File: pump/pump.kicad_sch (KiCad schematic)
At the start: 0 parts

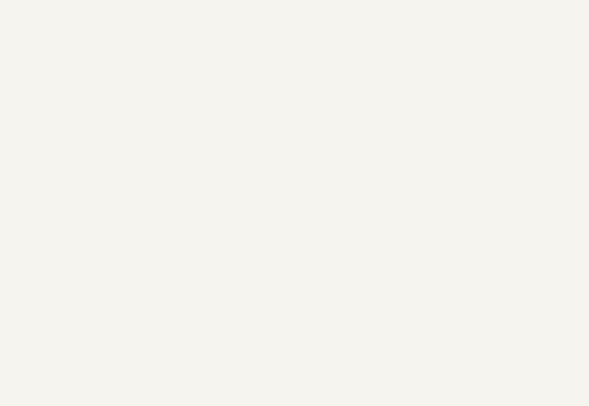
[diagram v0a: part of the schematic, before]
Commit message: Added control relays schematic
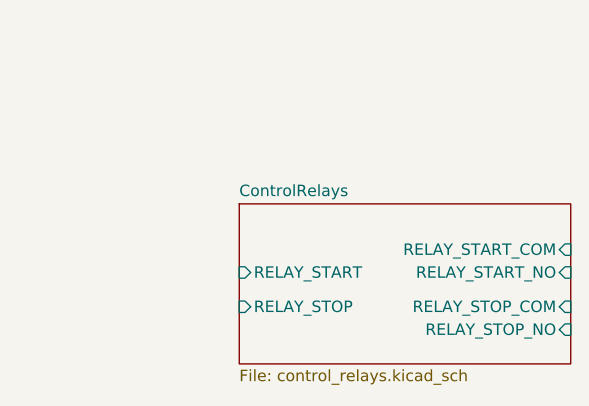
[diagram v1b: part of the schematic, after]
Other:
- added sheet ControlRelays (control_relays.kicad_sch)
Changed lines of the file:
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@@
+		)
+	)
+	(sheet
+		(at 228.6 144.78)
+		(size 36.83 17.78)
+		(exclude_from_sim no)
+		(in_bom yes)
+		(on_board yes)
+		(dnp no)
+		(fields_autoplaced yes)
+		(stroke
+			(width 0.1524)
+			(type solid)
+		)
+		(fill
+			(color 0 0 0 0.0000)
+		)
+		(property "Sheetname" "ControlRelays"
+			(at 228.6 144.0684 0)
+			(effects
+				(font
+					(size 1.27 1.27)
+				)
+				(justify left bottom)
+			)
+		)
+		(property "Sheetfile" "control_relays.kicad_sch"
+			(at 228.6 163.1446 0)
+			(effects
+				(font
+					(size 1.27 1.27)
+				)
+				(justify left top)
+			)
+		)
+		(pin "RELAY_START" input
+			(at 228.6 152.4 180)
+			(effects
+				(font
+					(size 1.27 1.27)
+				)
+				(justify left)
+			)
+		)
+		(pin "RELAY_START_COM" input
+			(at 265.43 149.86 0)
+			(effects
+				(font
+					(size 1.27 1.27)
+				)
+				(justify right)
+			)
+		)
+		(pin "RELAY_START_NO" input
+			(at 265.43 152.4 0)
+			(effects
+				(font
+					(size 1.27 1.27)
+				)
+				(justify right)
+			)
+		)
+		(pin "RELAY_STOP" input
+			(at 228.6 156.21 180)
+			(effects
+				(font
+					(size 1.27 1.27)
+				)
+				(justify left)
+			)
+		)
+		(pin "RELAY_STOP_COM" input
+			(at 265.43 156.21 0)
+			(effects
+				(font
+					(size 1.27 1.27)
+				)
+				(justify right)
+			)
+		)
+		(pin "RELAY_STOP_NO" input
+			(at 265.43 158.75 0)
+			(effects
+				(font
+					(size 1.27 1.27)
+				)
+				(justify right)
+			)
+		)
+		(instances
+			(project "pump"
+				(path "/e0be0fc6-35a9-4dbe-8638-3e88dcb86763"
+					(page "2")
+				)
+			)
 		)
 	)

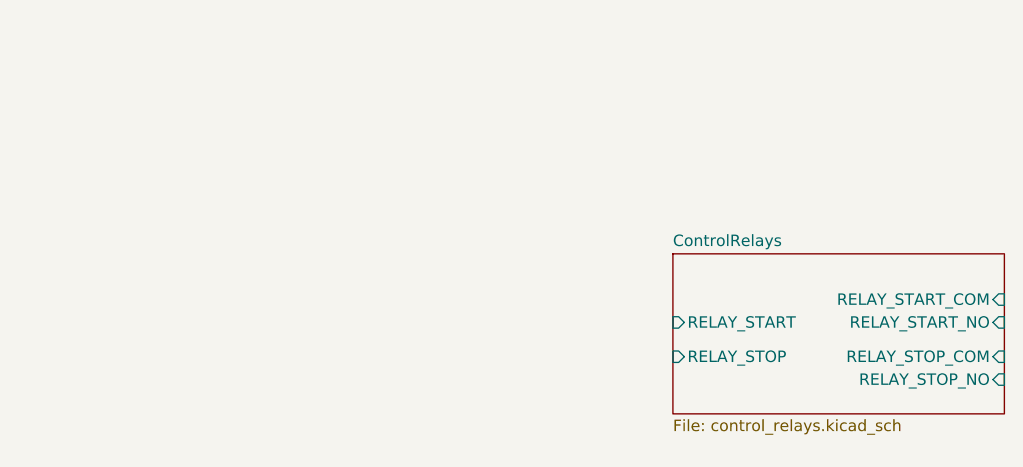
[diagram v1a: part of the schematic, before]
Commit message: added pressure sensor modulew
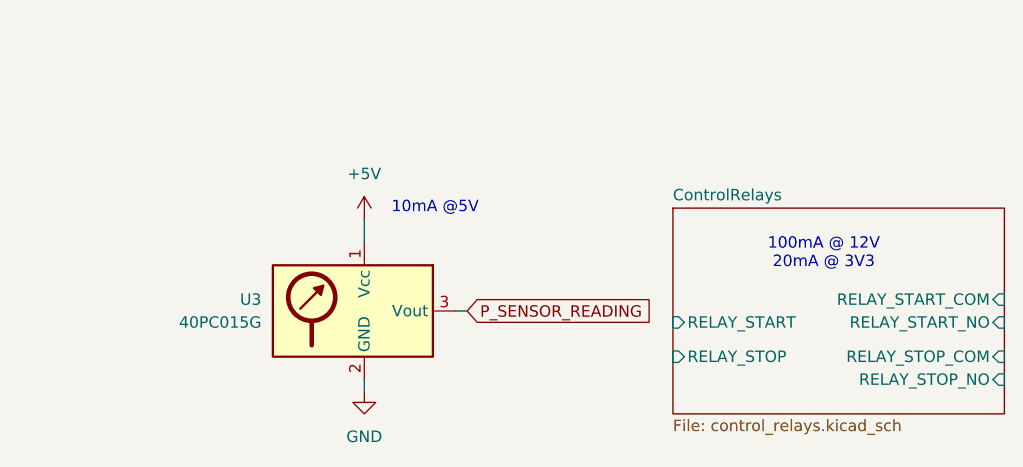
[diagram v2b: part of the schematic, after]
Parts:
- added U3: 40PC015G, symbol Sensor_Pressure:40PC015G
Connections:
- new net +5V: U3.1 (Vcc)
- new net GND: U3.2 (GND)
- new net P_SENSOR_READING: U3.3 (Vout)
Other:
- note added: "100mA @ 12V 20mA @ 3V3"
- note added: "10mA @5V"
